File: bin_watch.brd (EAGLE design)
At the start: 39.2 x 30.1 mm, 107 parts, among them IC1 MEGA48/88/168-MU, J1 USB3100-XX-X_REVB, Q1 32.768kHz, T1 2N7002BKV, T2 2N7002BKV, T3 2N7002BKV, T4 2N7002BKV, T5 PMDT670UPE, T6 PMDT670UPE, T7 PMDT670UPE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

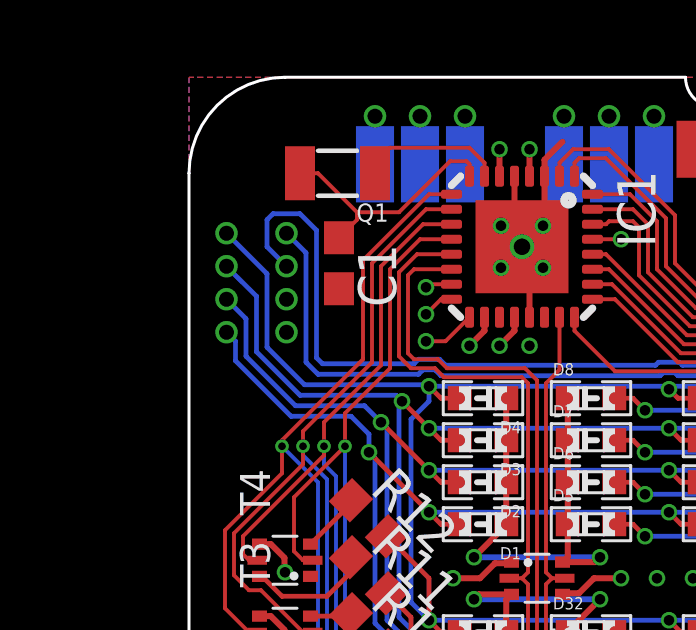
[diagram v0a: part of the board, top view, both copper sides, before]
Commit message: Made the external connctor smaller
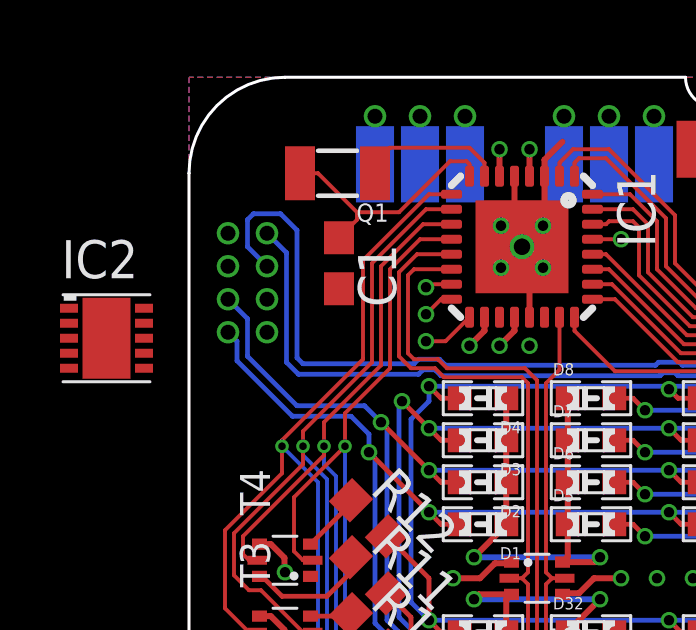
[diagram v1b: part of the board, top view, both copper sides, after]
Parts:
- added IC2: TINY13V-10MM0, atmel:10M1
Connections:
- net GND: now also IC2.11, IC2.5
- net MISO: now also IC2.7
- net MOSI: now also IC2.6
- net SCK: now also IC2.9
- net VCC: now also IC2.10
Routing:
- net LIGHT6: track 61.3 -> 62.5 mm
- net LIGHT3: track 77.0 -> 77.7 mm
- net LIGHT2: track 91.8 -> 92.4 mm
- net LIGHT1: track 70.4 -> 71.1 mm
- net LIGHT0: track 71.2 -> 71.8 mm

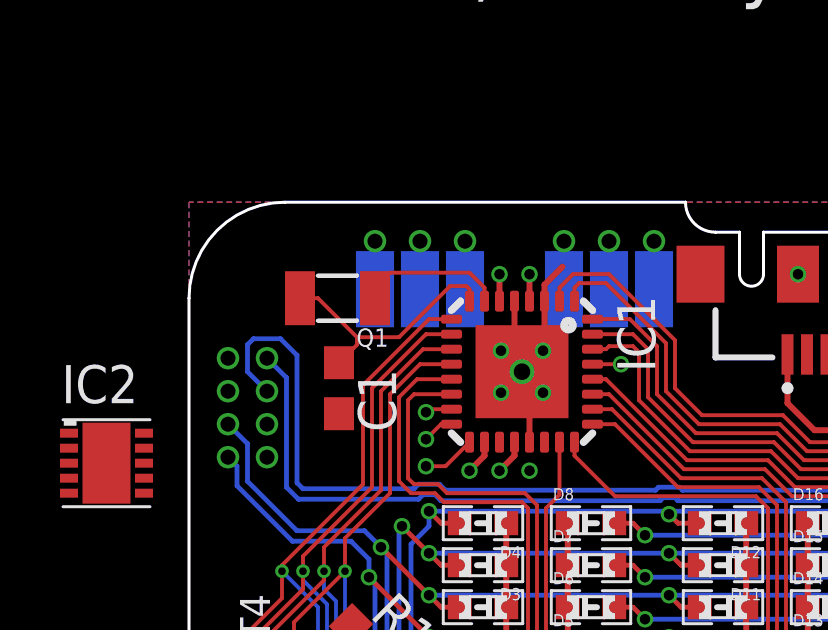
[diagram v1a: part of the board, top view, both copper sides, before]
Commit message: Crystal moved out of the way
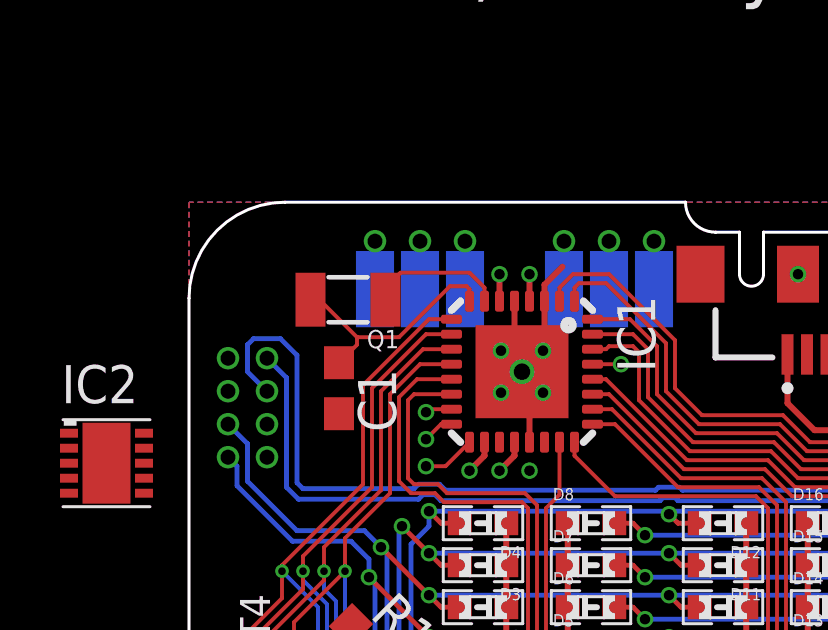
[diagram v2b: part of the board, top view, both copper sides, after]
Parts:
- moved Q1 0.35 mm to (5.30, 26.9)
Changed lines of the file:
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@@
 <element name="D13" library="standardparts" package="0603.LED" value="RG" x="21.4" y="15.2"/>
 <element name="IC1" library="avr-5" package="MLF32" value="MEGA48/88/168-MU" x="11.1" y="24.45" rot="R270"/>
-<element name="Q1" library="crystal-geyer_V1_0" library_urn="urn:adsk.eagle:library:203" package="3.2X1.5" value="32.768kHz" x="4.95" y="26.9" rot="R180"/>
+<element name="Q1" library="crystal-geyer_V1_0" library_urn="urn:adsk.eagle:library:203" package="3.2X1.5" value="32.768kHz" x="5.3" y="26.85" rot="R180"/>
 <element name="S1" library="SparkFun-Switches" library_urn="urn:adsk.eagle:library:535" package="TACTILE_SWITCH_SMD_5.2MM" value="select" x="11.7" y="3.2">
 <attribute name="PROD_ID" value="SWCH-08247" x="11.7" y="3.2" size="1.778" layer="27" display="off"/>
@@
 <contactref element="Q1" pad="1"/>
 <contactref element="IC1" pad="7"/>
-<wire x1="6.7" y1="27.75" x2="9.35" y2="27.75" width="0.13" layer="1"/>
+<wire x1="7.05" y1="27.75" x2="9.35" y2="27.75" width="0.13" layer="1"/>
 <wire x1="9.35" y1="27.75" x2="9.85" y2="27.25" width="0.13" layer="1"/>
 <wire x1="9.85" y1="27.25" x2="9.85" y2="26.8" width="0.13" layer="1"/>
-<wire x1="6.2" y1="26.9" x2="6.2" y2="27.25" width="0.13" layer="1"/>
-<wire x1="6.2" y1="27.25" x2="6.7" y2="27.75" width="0.13" layer="1"/>
+<wire x1="6.55" y1="26.85" x2="6.55" y2="27.25" width="0.13" layer="1"/>
+<wire x1="6.55" y1="27.25" x2="7.05" y2="27.75" width="0.13" layer="1"/>
 </signal>
 <signal name="GND" class="1">
@@
 <wire x1="7" y1="25.6" x2="5.6" y2="25.6" width="0.13" layer="1"/>
 <wire x1="7" y1="25.6" x2="8.7" y2="27.3" width="0.13" layer="1"/>
-<wire x1="3.7" y1="26.9" x2="4.3" y2="26.9" width="0.13" layer="1"/>
-<wire x1="4.3" y1="26.9" x2="5.6" y2="25.6" width="0.13" layer="1"/>
+<wire x1="4.05" y1="26.85" x2="4.35" y2="26.85" width="0.13" layer="1"/>
+<wire x1="4.35" y1="26.85" x2="5.6" y2="25.6" width="0.13" layer="1"/>
 <wire x1="5.6" y1="25.6" x2="5.6" y2="25.35" width="0.13" layer="1"/>
 <wire x1="5.6" y1="25.35" x2="5" y2="24.75" width="0.13" layer="1"/>

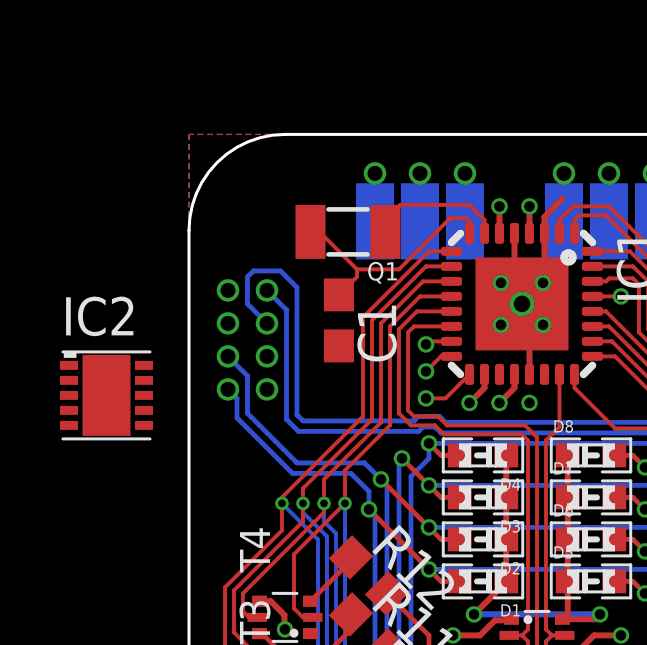
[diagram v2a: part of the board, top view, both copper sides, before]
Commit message: Moved connector up
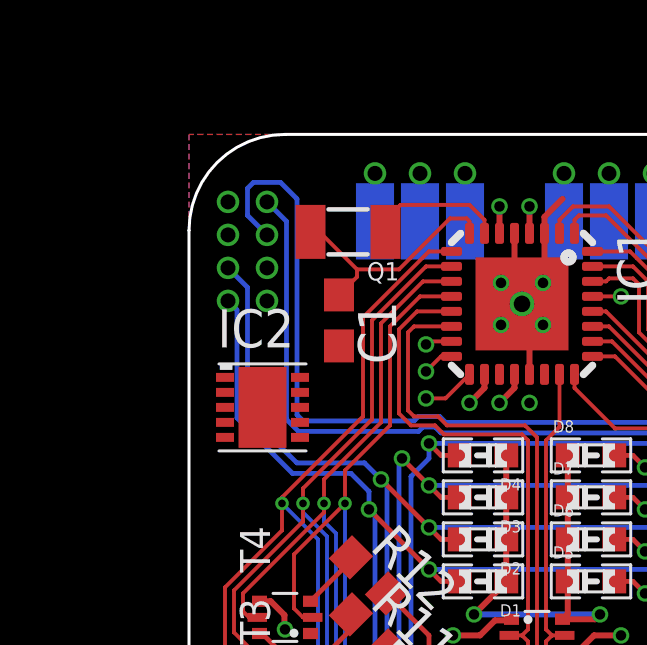
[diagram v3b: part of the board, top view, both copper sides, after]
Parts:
- moved IC2 5.22 mm to (2.45, 21.0)
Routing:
- net LIGHT5: track 61.4 -> 64.3 mm
- net LIGHT3: track 77.7 -> 80.6 mm
- net LIGHT2: track 92.4 -> 95.4 mm
- net LIGHT4: track 61.6 -> 64.6 mm
- net LIGHT1: track 71.1 -> 74.0 mm
- net LIGHT0: track 71.8 -> 74.4 mm
- net LIGHT6: track 62.5 -> 64.8 mm
- net LIGHT7: track 61.4 -> 63.7 mm

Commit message: Moved crystal
TODO: Pick existing uC for ISP
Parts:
- moved C1 3.12 mm to (7.00, 26.3), turned to 225 degrees
- moved Q1 1.04 mm to (4.45, 27.4), turned to 270 degrees
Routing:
- net MISO: track 1.06 -> 7.23 mm, vias 1 -> 2
- net SCK: track 1.78 -> 6.52 mm, vias 1 -> 2
- net XTAL_P: track 4.56 -> 7.52 mm
- net MOSI: track 0.89 -> 3.39 mm, vias 1 -> 2

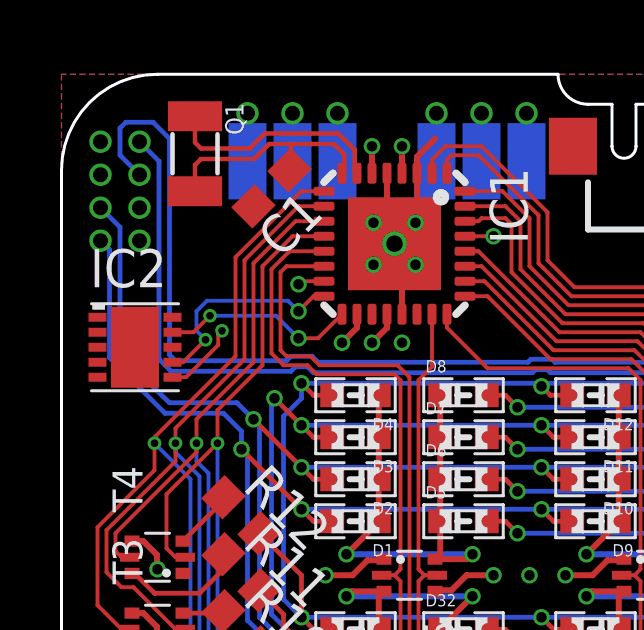
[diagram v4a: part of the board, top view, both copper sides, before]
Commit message: Fixed undocumented clearance violations
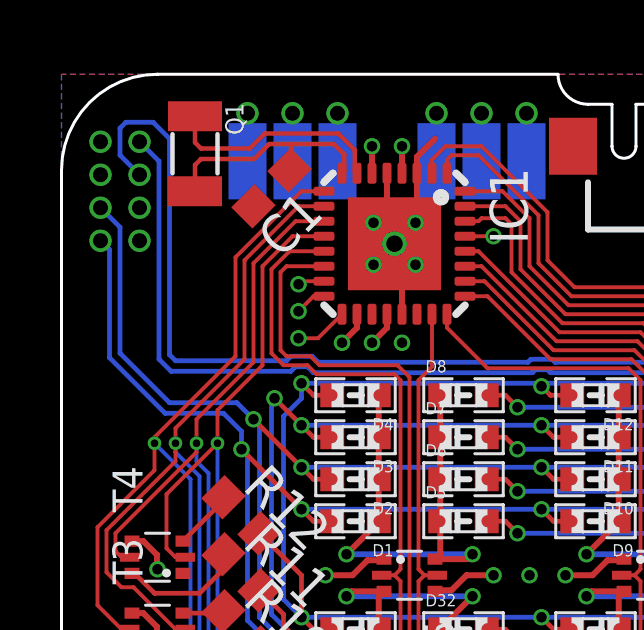
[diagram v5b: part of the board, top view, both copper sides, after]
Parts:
- removed IC2: TINY13V-10MM0, atmel:10M1
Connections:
- net GND: no longer IC2.11, IC2.5
- net MISO: no longer IC2.7
- net MOSI: no longer IC2.6
- net SCK: no longer IC2.9
- net VCC: no longer IC2.10
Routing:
- net MISO: track 7.23 -> 1.06 mm, vias 2 -> 1
- net SCK: track 6.52 -> 1.78 mm, vias 2 -> 1
- net MOSI: track 3.39 -> 0.89 mm, vias 2 -> 1
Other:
- board text added: "RST"

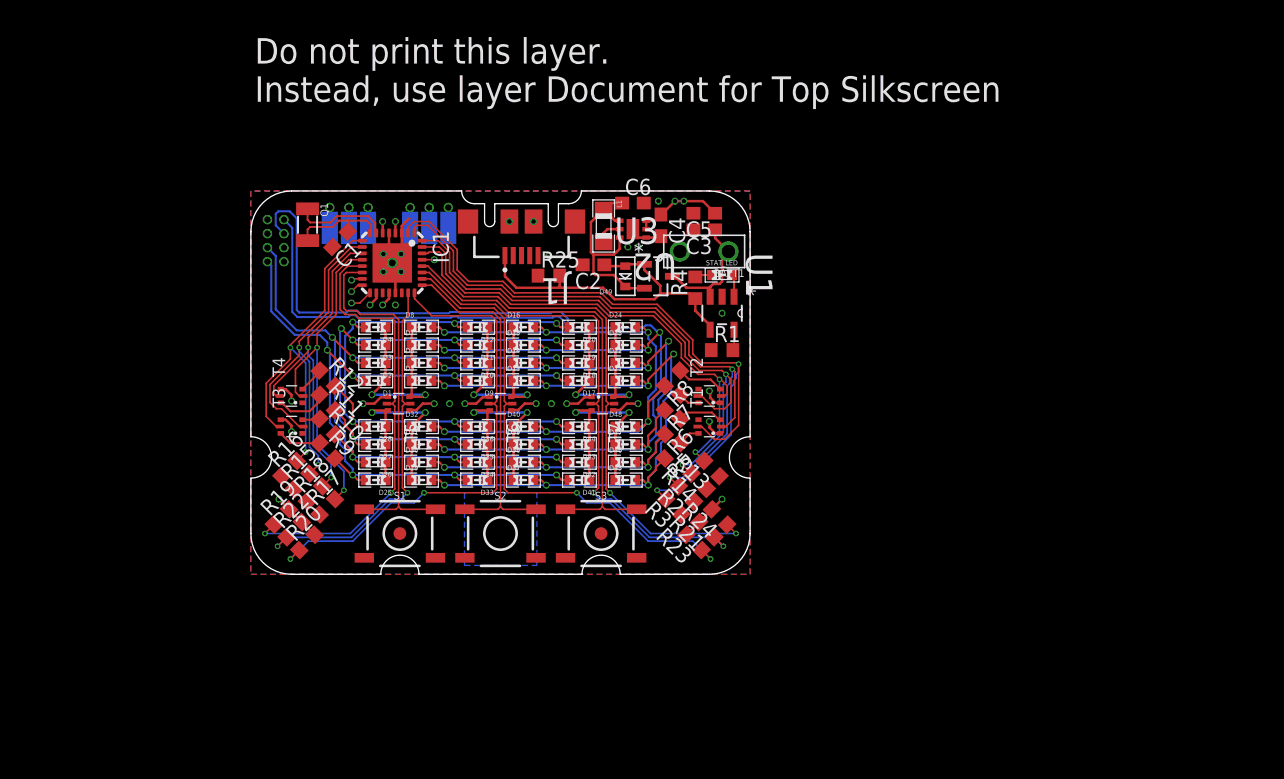
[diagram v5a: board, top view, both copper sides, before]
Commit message: Replaced 328p with 4x4mm VQFN
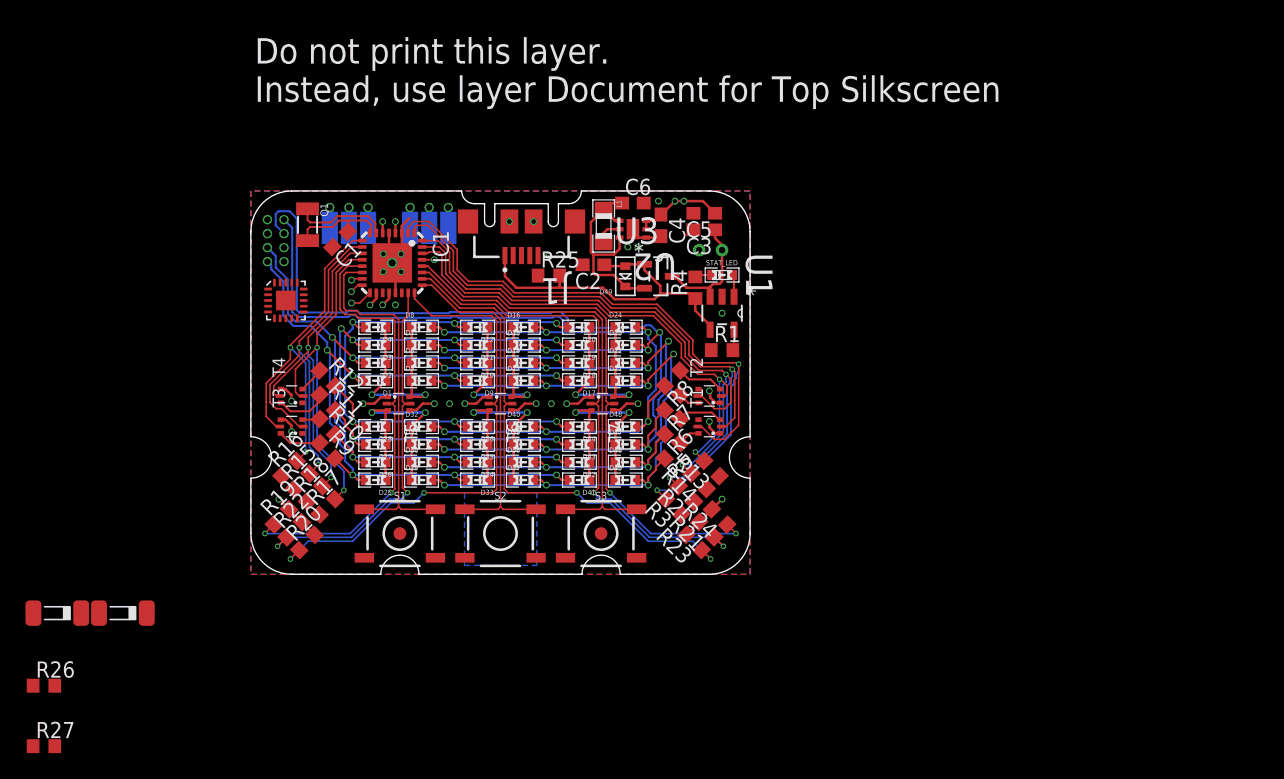
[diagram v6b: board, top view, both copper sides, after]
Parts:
- removed BATT1: 56455 201 012, SparkFun-Connectors:1X02_BIG
- added R26, R27: 68, rcl:R0603
- added U$3, U$4: BZV55-C3V6, pmg-library:SOD-80
- added U4: ATTINY44A-MMH, Atmel_By_element14_Batch_1-00:VQFN20P300X300
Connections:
- new net N$2: R26.2, U$3.C, U4.14, U4.15
- new net N$3: R27.2, U$4.C, U4.5
- net D_N: now also R27.1
- net D_P: now also R26.1
- net GND: now also U$3.A, U$4.A, U4.8, U4.EP; no longer BATT1.P$2
- net MISO: now also U4.20
- net MOSI: now also U4.16
- net RST: now also U4.2
- net SCK: now also U4.1
- net VBATT: no longer BATT1.P$1
- net VBUS: now also U4.9
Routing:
- net VBATT: track 9.94 -> 9.53 mm, vias 0 -> 1
- net GND: vias 19 -> 20

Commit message: Lot of other changes
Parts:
- removed IC1: MEGA48/88/168-MU, avr-5:MLF32
- removed U4: ATTINY44A-MMH, Atmel_By_element14_Batch_1-00:VQFN20P300X300
- added U$5: MEGA328P-MMH, avr-5:VQFN28
- moved R27 57.4 mm to (19.8, 31.1), turned to 180 degrees
- moved U$4 52.7 mm to (23.1, 33.1), turned to 180 degrees
- moved R26 50.3 mm to (13.8, 31.5), turned to 180 degrees
- moved U$3 43.6 mm to (13.8, 33.4)
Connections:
- removed net ADC6: IC1.19
- removed net ADC7: IC1.22
- new net N$10: U$5.26
- new net N$11: U$5.27
- new net N$12: U$5.1
- new net N$13: U$5.7
- new net N$14: U$5.8
- new net N$15: U$5.9
- new net N$16: U$5.10
- new net N$17: U$5.11
- new net N$18: U$5.12
- new net N$4: U$5.19
- new net N$5: U$5.20
- new net N$6: U$5.21
- new net N$7: U$5.22
- new net N$8: U$5.23
- new net N$9: U$5.24
- net BTN1: no longer IC1.14
- net BTN2: no longer IC1.25
- net BTN3: no longer IC1.28
- net D_N: now also R26.1, U$3.C; no longer R27.1
- net D_P: now also R27.1, U$4.C; no longer R26.1
- net GND: now also U$5.18, U$5.4, U$5.EP; no longer IC1.21, IC1.3, IC1.5, U4.8, U4.EP
- net G_BLOCK0: no longer IC1.13
- net G_BLOCK1: no longer IC1.24
- net G_BLOCK2: no longer IC1.27
- net G_BLOCK3: no longer IC1.23
- net G_BLOCK4: no longer IC1.26
- net G_BLOCK5: no longer IC1.30
- net G_LIGHT0: no longer IC1.1
- net G_LIGHT1: no longer IC1.2
- net G_LIGHT2: no longer IC1.31
- net G_LIGHT3: no longer IC1.32
- net G_LIGHT4: no longer IC1.10
- net G_LIGHT5: no longer IC1.9
- net G_LIGHT6: no longer IC1.12
- net G_LIGHT7: no longer IC1.11
- net MISO: now also U$5.14; no longer IC1.16, U4.20
- net MOSI: now also U$5.13; no longer IC1.15, U4.16
- net N$2: now also U$5.2; no longer U$3.C, U4.14, U4.15
- net N$3: now also U$5.28; no longer U$4.C, U4.5
- net RST: now also U$5.25; no longer IC1.29, U4.2
- net SCK: now also U$5.15; no longer IC1.17, U4.1
- net VBUS: no longer U4.9
- net VCC: now also U$5.16, U$5.17, U$5.3; no longer IC1.18, IC1.20, IC1.4, IC1.6
- net XTAL_N: now also U$5.6; no longer IC1.8
- net XTAL_P: now also U$5.5; no longer IC1.7
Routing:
- net GND: track 31.4 -> 8.31 mm, vias 20 -> 14
- net VCC: track 32.3 -> 28.1 mm, vias 14 -> 10
- net SCK: track 1.78 -> 0.00 mm, vias 1 -> 0
- net G_BLOCK3: track 29.6 -> 27.8 mm
- net G_LIGHT2: track 38.8 -> 37.5 mm
- net G_LIGHT3: track 45.3 -> 44.0 mm
- net BTN1: track 29.3 -> 28.0 mm
- net G_BLOCK0: track 35.9 -> 34.8 mm
- net MISO: track 1.06 -> 0.00 mm, vias 1 -> 0
- net G_LIGHT6: track 27.0 -> 25.9 mm
- net G_LIGHT7: track 26.9 -> 26.0 mm
- net RST: track 0.95 -> 0.00 mm, vias 1 -> 0
- net MOSI: track 0.89 -> 0.00 mm, vias 1 -> 0
- net G_LIGHT4: track 29.9 -> 29.1 mm
- net G_LIGHT5: track 28.5 -> 27.7 mm
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- removed copper zone on layer 16, net GND
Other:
- board text removed: "GND"
- board text removed: "MISO"
- board text removed: "MOSI"
- board text removed: "SCK"
- board text removed: "Vcc"
